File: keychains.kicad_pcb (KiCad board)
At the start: 2 copper layers, 220.8 x 105.3 mm, 311 parts

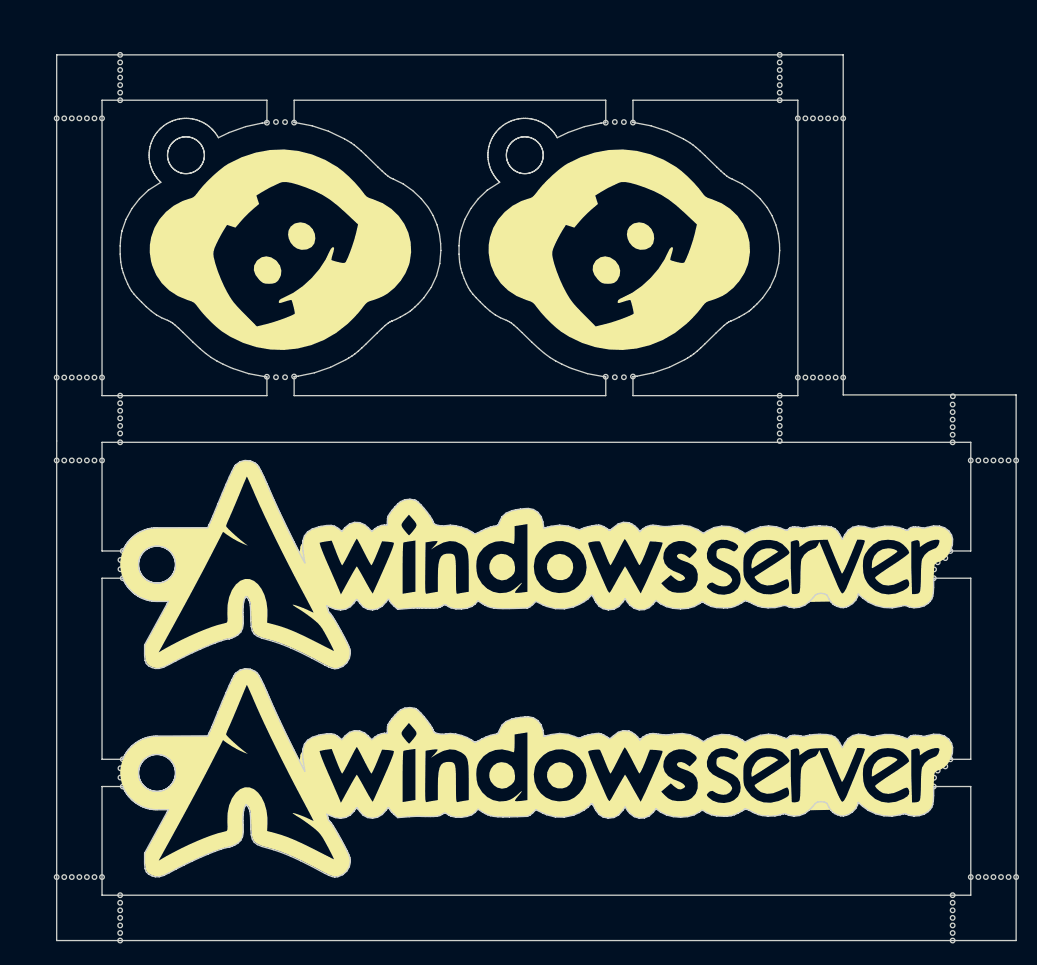
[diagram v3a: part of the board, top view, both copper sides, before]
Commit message: panel resize
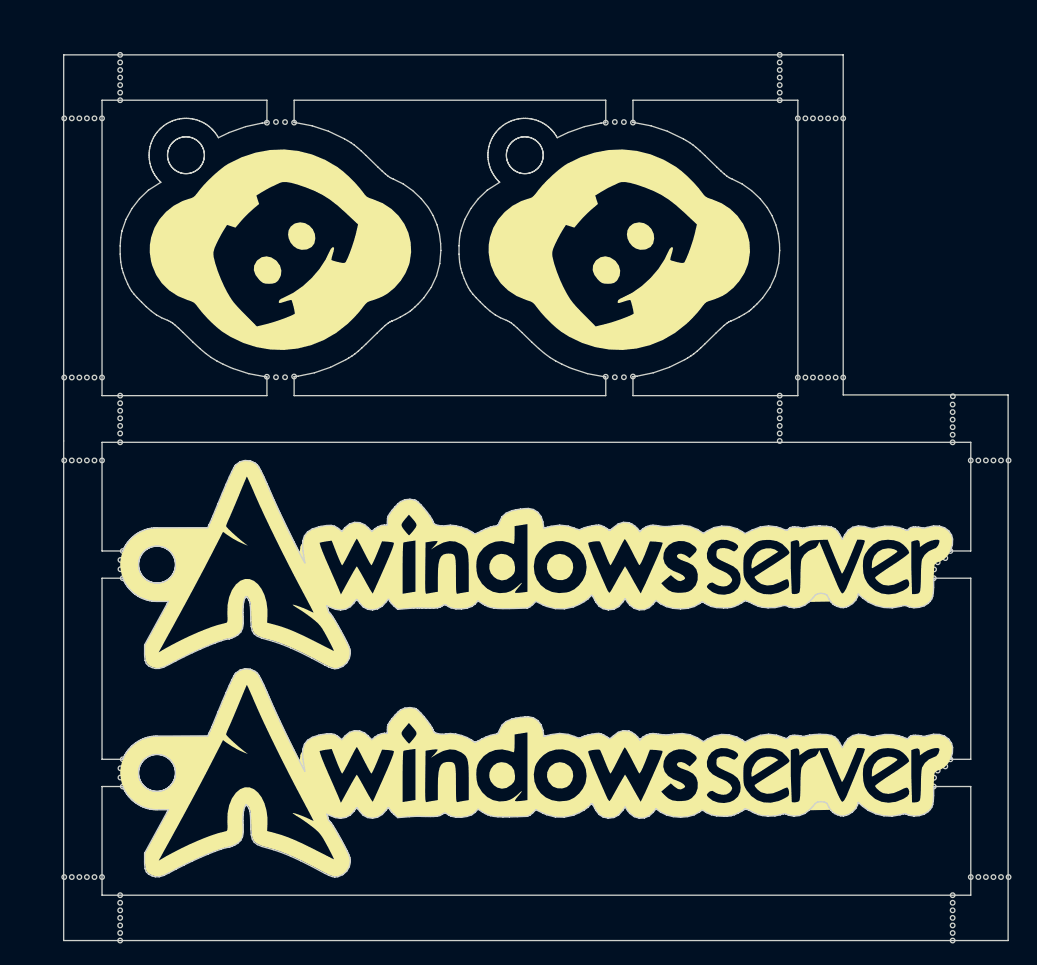
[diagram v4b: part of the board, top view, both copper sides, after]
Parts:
- removed the KiKit_MB_10_1 at (264.7, 69.0)
- removed the KiKit_MB_10_1 at (264.7, 124.1)
- removed the KiKit_MB_11_7 at (370.5, 78.2)
- removed the KiKit_MB_12_7 at (370.5, 124.1)
- removed the KiKit_MB_9_1 at (264.7, 78.2)
- removed the KiKit_MB_9_1 at (264.7, 40.5)
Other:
- board size 220.8 x 105.3 mm -> 219.9 x 105.3 mm
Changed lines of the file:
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@@
   )
   (footprint "NPTH" (layer "F.Cu")
-    (at 264.657743 78.175395)
-    (attr through_hole)
-    (fp_text reference "KiKit_MB_9_1" (at 0 0.5) (layer "F.SilkS") hide
-        (effects (font (size 1 1) (thickness 0.15)))
-    )
-    (fp_text value "NPTH" (at 0 -0.5) (layer "F.Fab") hide
-        (effects (font (size 1 1) (thickness 0.15)))
-    )
-    (pad "" np_thru_hole circle (at 0 0) (size 0.5 0.5) (drill 0.5) (layers "*.Mask"))
-  )
-  (footprint "NPTH" (layer "F.Cu")
     (at 326.203525 68.999937)
     (attr through_hole)
@@
   )
   (footprint "NPTH" (layer "F.Cu")
-    (at 370.452714 78.175395)
-    (attr through_hole)
-    (fp_text reference "KiKit_MB_11_7" (at 0 0.5) (layer "F.SilkS") hide
-        (effects (font (size 1 1) (thickness 0.15)))
-    )
-    (fp_text value "NPTH" (at 0 -0.5) (layer "F.Fab") hide
-        (effects (font (size 1 1) (thickness 0.15)))
-    )
-    (pad "" np_thru_hole circle (at 0 0) (size 0.5 0.5) (drill 0.5) (layers "*.Mask"))
-  )
-  (footprint "NPTH" (layer "F.Cu")
     (at 234.736653 61.58)
     (attr through_hole)
@@
   )
   (footprint "NPTH" (layer "F.Cu")
-    (at 264.657743 69.030801)
-    (attr through_hole)
-    (fp_text reference "KiKit_MB_10_1" (at 0 0.5) (layer "F.SilkS") hide
-        (effects (font (size 1 1) (thickness 0.15)))
-    )
-    (fp_text value "NPTH" (at 0 -0.5) (layer "F.Fab") hide
-        (effects (font (size 1 1) (thickness 0.15)))
-    )
-    (pad "" np_thru_hole circle (at 0 0) (size 0.5 0.5) (drill 0.5) (layers "*.Mask"))
-  )
-  (footprint "NPTH" (layer "F.Cu")
     (at 157.302514 127.951802)
     (attr through_hole)
@@
   )
   (footprint "NPTH" (layer "F.Cu")
-    (at 264.657743 124.115937)
-    (attr through_hole)
-    (fp_text reference "KiKit_MB_10_1" (at 0 0.5) (layer "F.SilkS") hide
-        (effects (font (size 1 1) (thickness 0.15)))
-    )
-    (fp_text value "NPTH" (at 0 -0.5) (layer "F.Fab") hide
-        (effects (font (size 1 1) (thickness 0.15)))
-    )
-    (pad "" np_thru_hole circle (at 0 0) (size 0.5 0.5) (drill 0.5) (layers "*.Mask"))
-  )
-  (footprint "NPTH" (layer "F.Cu")
     (at 349.717716 40.454263)
     (attr through_hole)
@@
   )
   (footprint "NPTH" (layer "F.Cu")
-    (at 370.452714 124.115937)
-    (attr through_hole)
-    (fp_text reference "KiKit_MB_12_7" (at 0 0.5) (layer "F.SilkS") hide
-        (effects (font (size 1 1) (thickness 0.15)))
-    )
-    (fp_text value "NPTH" (at 0 -0.5) (layer "F.Fab") hide
-        (effects (font (size 1 1) (thickness 0.15)))
-    )
-    (pad "" np_thru_hole circle (at 0 0) (size 0.5 0.5) (drill 0.5) (layers "*.Mask"))
-  )
-  (footprint "NPTH" (layer "F.Cu")
     (at 156.67668 27.670129)
     (attr through_hole)
@@
   )
   (footprint "NPTH" (layer "F.Cu")
-    (at 264.657743 40.454263)
-    (attr through_hole)
-    (fp_text reference "KiKit_MB_9_1" (at 0 0.5) (layer "F.SilkS") hide
-        (effects (font (size 1 1) (thickness 0.15)))
-    )
-    (fp_text value "NPTH" (at 0 -0.5) (layer "F.Fab") hide
-        (effects (font (size 1 1) (thickness 0.15)))
-    )
-    (pad "" np_thru_hole circle (at 0 0) (size 0.5 0.5) (drill 0.5) (layers "*.Mask"))
-  )
-  (footprint "NPTH" (layer "F.Cu")
     (at 229.40332 28.503462)
     (attr through_hole)
@@
       )
       (stroke (width 0) (type solid)) (fill solid) (layer "F.Mask"))
-    (group "" (id 691000f7-2b6a-46af-911b-88de9f91fc23)
-      (members
-        003f2d02-a2f4-4158-ab84-58441fb2d8f7
-        0a86a417-0db7-4872-b687-df024ca11ac6
-        12bcc803-e175-41a3-9038-585a5fce6ed6
-        6af657c5-8f64-4c95-9b4f-8277dde83b88
-        82c25bfb-c6c8-4d7f-8687-3d5fac7ad0ae
-        aff589b4-0746-4d34-866d-a377b0f80bce
-        b59a0ad6-1b9d-4ae6-b34a-1f2f4e371c08
-        e419ab5e-5027-42e9-a031-120d0ddec652
-        e7295f1f-a336-4f5d-928c-24105668f8b4
-        ebab1c1a-fdfa-490b-bf80-17506b5d1ef1
-        f37d7b2c-bbeb-4c65-ac5f-6de722a6a46f
-        fc8b9ac3-b61d-4c0e-978b-0b0b55675f64
-        fe0b5a2e-d2ec-48dd-b757-ad92609d427e
-      )
-    )
-    (group "" (id 1434eff9-0f7e-48ee-9a8b-52ae86a42e45)
-      (members
-        01efa762-c6c9-4b40-85cd-622a5a89796e
-        0d007a0d-48b5-4838-81f2-3dfa95b90ef8
-        34532e25-d586-4b85-b84b-96349a9cb3e5
-        4402e00a-638e-40c7-9917-4ab160fcc82a
-        4618c606-738e-45b7-8801-d48d89a36fb7
-        5ebdd965-ba64-4180-a234-e3a664141a7b
-        74c0dd39-efd9-44b1-b15f-2d84b1c8db80
-        8b55931c-25ee-447f-9dd9-e564e5c0d4aa
-        9060ae0d-e0a2-4df0-9f3d-1ad08bbc870a
-        a55b465b-8f30-4212-8da6-1b73f79fad49
-        c41d3c88-5cf2-4b6e-945e-dd52c0c65efd
-        c788e498-9ee8-4fb7-a000-3ba24c43b29d
-        d288d8cc-e37d-4339-b110-d20e33f31893
-      )
-    )
   )
   (footprint "NPTH" (layer "F.Cu")
@@
   (gr_line (start 163.049541 88.692986) (end 163.103697 88.777671)
     (stroke (width 0.1) (type default)) (layer "Edge.Cuts"))
-  (gr_line (start 370.452714 131.115937) (end 370.452714 131.115937)
-    (stroke (width 0.1) (type default)) (layer "Edge.Cuts"))
   (gr_line (start 161.838388 91.805877) (end 161.740082 91.826858)
     (stroke (width 0.1) (type default)) (layer "Edge.Cuts"))
@@
   (gr_line (start 352.774542 116.556029) (end 352.973287 116.163128)
     (stroke (width 0.1) (type default)) (layer "Edge.Cuts"))
-  (gr_line (start 264.657743 33.454263) (end 264.657743 76.030801)
+  (gr_line (start 265.43 33.454263) (end 265.43 76.030801)
     (stroke (width 0.1) (type default)) (layer "Edge.Cuts"))
   (gr_line (start 277.218154 88.287216) (end 277.284237 88.362962)
@@
   (gr_line (start 280.921582 44.219837) (end 280.933983 44.319589)
     (stroke (width 0.1) (type default)) (layer "Edge.Cuts"))
-  (gr_line (start 264.657743 76.030801) (end 264.657743 131.115937)
+  (gr_line (start 265.43 76.030801) (end 265.43 131.115937)
     (stroke (width 0.1) (type default)) (layer "Edge.Cuts"))
   (gr_line (start 355.879486 117.363723) (end 356.786489 117.40495)
@@
   (gr_line (start 275.315835 93.704335) (end 275.517905 93.719478)
     (stroke (width 0.1) (type default)) (layer "Edge.Cuts"))
-  (gr_line (start 370.452714 70.950801) (end 351.384383 70.950801)
+  (gr_line (start 369.57 70.950801) (end 351.384383 70.950801)
     (stroke (width 0.1) (type default)) (layer "Edge.Cuts"))
   (gr_line (start 274.403669 111.08321) (end 274.481814 111.019982)
@@
   (gr_line (start 185.684834 94.714949) (end 186.20375 94.414455)
     (stroke (width 0.1) (type default)) (layer "Edge.Cuts"))
-  (gr_line (start 264.657743 131.115937) (end 370.452714 131.115937)
+  (gr_line (start 265.43 131.115937) (end 369.57 131.115937)
     (stroke (width 0.1) (type default)) (layer "Edge.Cuts"))
   (gr_line (start 329.456194 117.599067) (end 329.992761 117.376868)
@@
   (gr_line (start 215.749171 108.482629) (end 215.418548 108.587857)
     (stroke (width 0.1) (type default)) (layer "Edge.Cuts"))
-  (gr_line (start 351.384383 33.454263) (end 264.657743 33.454263)
+  (gr_line (start 351.384383 33.454263) (end 265.43 33.454263)
     (stroke (width 0.1) (type default)) (layer "Edge.Cuts"))
   (gr_line (start 274.348244 121.489403) (end 274.348244 122.429486)
@@
   (gr_line (start 315.753369 46.484165) (end 315.656889 46.455953)
     (stroke (width 0.1) (type default)) (layer "Edge.Cuts"))
-  (gr_line (start 370.452714 131.115937) (end 370.452714 70.950801)
+  (gr_line (start 369.57 131.115937) (end 369.57 70.950801)
     (stroke (width 0.1) (type default)) (layer "Edge.Cuts"))
   (gr_line (start 171.599448 116.990667) (end 171.652914 117.328449)

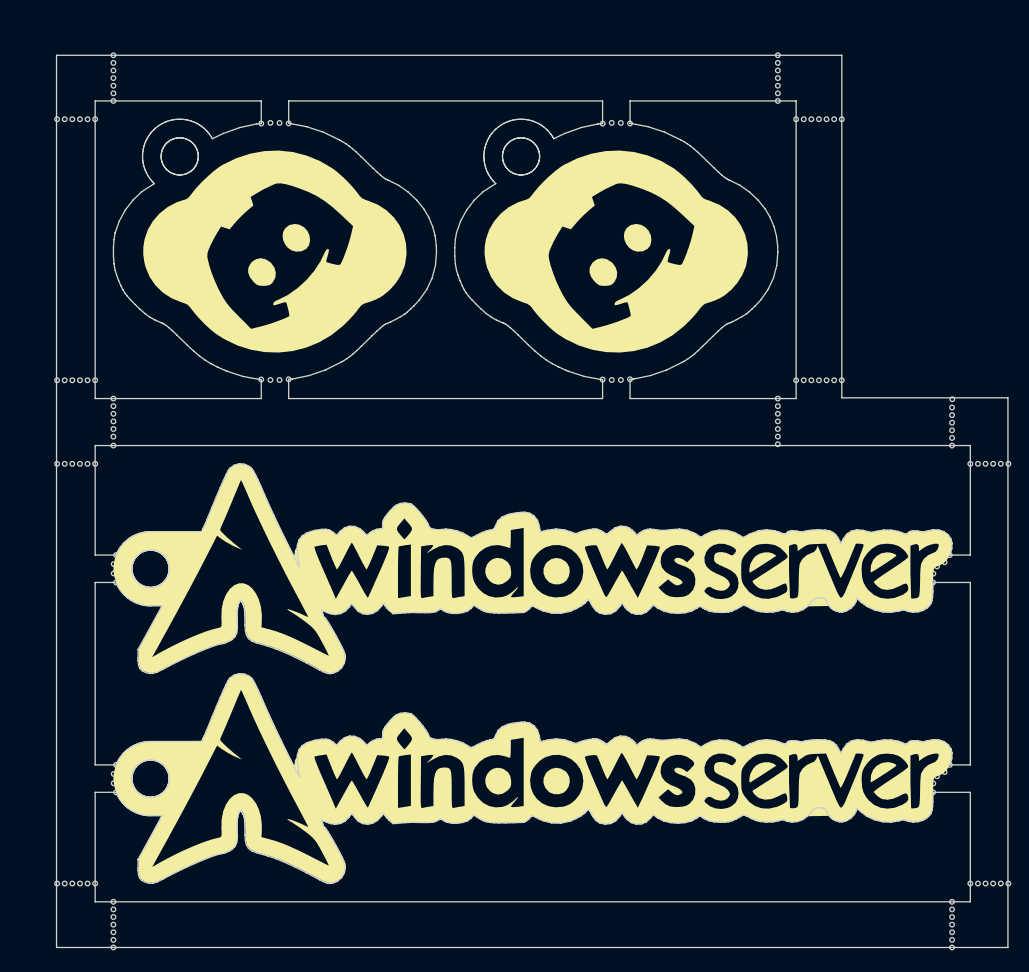
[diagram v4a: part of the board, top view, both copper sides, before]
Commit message: panel resize
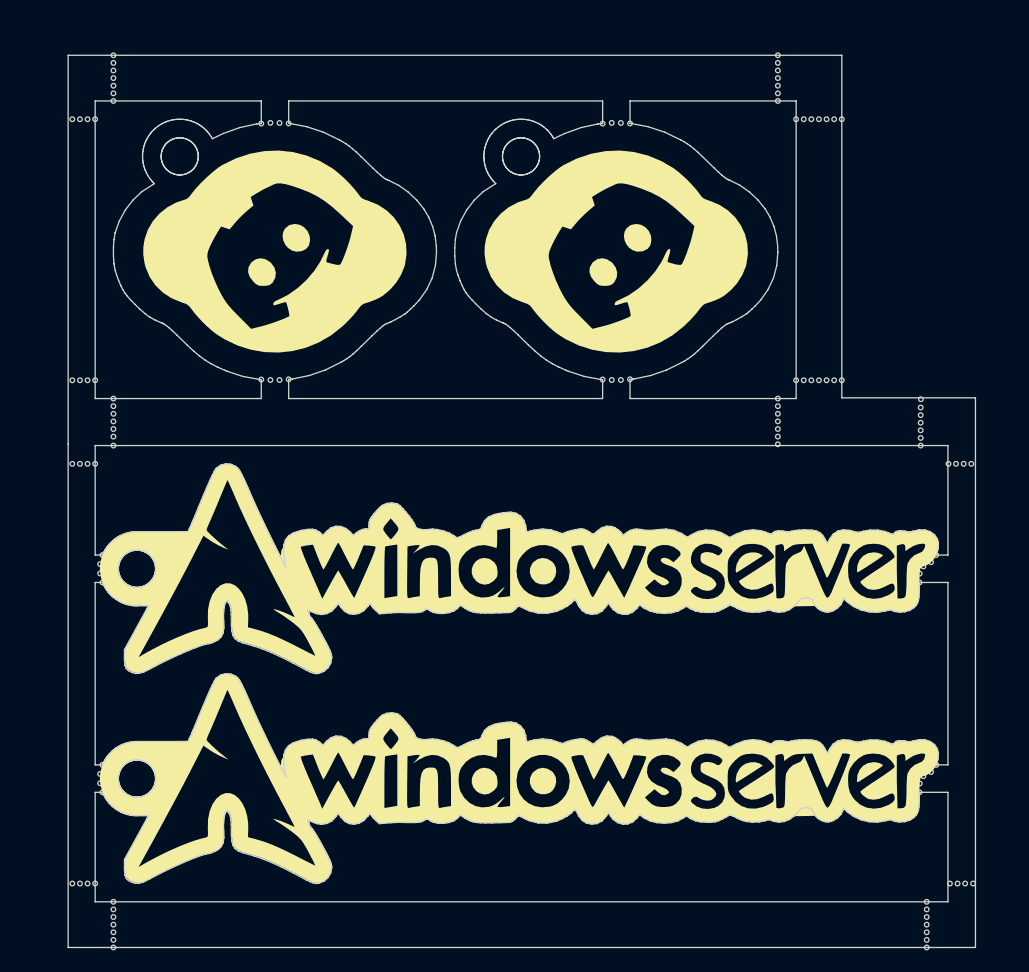
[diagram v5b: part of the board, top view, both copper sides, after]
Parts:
- removed the KiKit_MB_10_2 at (265.5, 69.0)
- removed the KiKit_MB_10_2 at (265.5, 124.1)
- removed the KiKit_MB_10_3 at (266.3, 69.0)
- removed the KiKit_MB_10_3 at (266.3, 124.1)
- removed the KiKit_MB_11_1 at (365.5, 78.2)
- removed the KiKit_MB_11_6 at (369.6, 78.2)
- removed the KiKit_MB_12_5 at (368.8, 124.1)
- removed the KiKit_MB_12_6 at (369.6, 124.1)
- removed the KiKit_MB_9_2 at (265.5, 40.5)
- removed the KiKit_MB_9_2 at (265.5, 78.2)
- removed the KiKit_MB_9_3 at (266.3, 40.5)
- removed the KiKit_MB_9_3 at (266.3, 78.2)
- moved KiKit_MB_6_1 3.43 mm to (360.0, 71.1)
- moved KiKit_MB_6_2 3.43 mm to (360.0, 72.0)
- moved KiKit_MB_6_3 3.43 mm to (360.0, 72.8)
- moved KiKit_MB_6_4 3.43 mm to (360.0, 73.7)
- moved KiKit_MB_6_5 3.43 mm to (360.0, 74.5)
- moved KiKit_MB_6_6 3.43 mm to (360.0, 75.3)
- moved KiKit_MB_6_7 3.43 mm to (360.0, 76.2)
- moved KiKit_MB_11_2 3.22 mm to (363.1, 78.2)
- moved KiKit_MB_11_3 3.22 mm to (363.9, 78.2)
- moved KiKit_MB_11_4 3.22 mm to (364.7, 78.2)
- moved KiKit_MB_11_5 3.22 mm to (365.6, 78.2)
- moved KiKit_MB_8_1 2.77 mm to (360.7, 126.1)
- moved KiKit_MB_8_2 2.77 mm to (360.7, 126.9)
- moved KiKit_MB_8_3 2.77 mm to (360.7, 127.8)
- moved KiKit_MB_8_4 2.77 mm to (360.7, 128.6)
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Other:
- board size 219.9 x 105.3 mm -> 216.3 x 105.3 mm
